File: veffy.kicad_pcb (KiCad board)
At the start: 4 copper layers, 83 parts, among them J1 SWD, Q1 2N7002, Q2 BFR93A, Q3 2N7002, Q4 BFR93AE6327HTSA1, U1 ATSAMD21G18A-A, U4 MC3361, U6 LM358_DFN, U7 AD9834, U8 QPA9510, Y2 TCXO-14

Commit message: rx pre-selector done
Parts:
- added C41: 100pF, Capacitor_SMD:C_0603_1608Metric, F.Cu at (116.0, 69.1)
- added L10: 13nH, Inductor_SMD:L_0603_1608Metric, F.Cu at (116.0, 71.6)
- added L15: 280nH, Inductor_SMD:L_0603_1608Metric, F.Cu at (116.0, 74.1)
- C20: value 30pF -> 10.9pF
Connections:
- net ANT renamed Net-(J2-In)
- C20 pad 1: Net-(C19-Pad1) -> AGND
- C20 pad 2: AGND -> TX_BAND_INT
- D2 pad 1: Net-(Q1-G) -> Net-(Q1-S)
- L4 pad 2: Net-(Q1-S) -> Net-(Q1-D)
- Q1 pad 1: Net-(Q1-G) -> RX_EN
- Q1 pad 3: RX_EN -> Net-(Q1-D)
- U8 pad 10: unconnected-(U8-RFOUT-Pad10) -> PA_DIE_OUT
- U8 pad 11: unconnected-(U8-RFOUT-Pad11) -> PA_DIE_OUT
- U8 pad 12: unconnected-(U8-RFOUT-Pad12) -> PA_DIE_OUT
- U8 pad 15: unconnected-(U8-APC2-Pad15) -> Net-(U8-APC2)
- U8 pad 16: unconnected-(U8-APC1-Pad16) -> Net-(U8-APC1)
- U8 pad 17: unconnected-(U8-EP-Pad17) -> AGND
- U8 pad 3: BAND_OUT -> Net-(U8-RFIN)
- U8 pad 5: unconnected-(U8-VCC2-Pad5) -> Net-(L10-Pad1)
- U8 pad 9: unconnected-(U8-RFOUT-Pad9) -> PA_DIE_OUT

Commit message: usb c done
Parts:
- added C43: 35.4pF, Capacitor_SMD:C_0603_1608Metric_Pad1.08x0.95mm_HandSolder, F.Cu at (96.1, 80.1)
- added C44: 10.9pF, Capacitor_SMD:C_0603_1608Metric_Pad1.08x0.95mm_HandSolder, F.Cu at (96.1, 82.6)
- added C45: C, Capacitor_SMD:C_0603_1608Metric_Pad1.08x0.95mm_HandSolder, F.Cu at (96.1, 85.1)
- added C46: 22pF, Capacitor_SMD:C_0603_1608Metric_Pad1.08x0.95mm_HandSolder, F.Cu at (96.1, 87.6)
- added C47: 27pF, Capacitor_SMD:C_0603_1608Metric_Pad1.08x0.95mm_HandSolder, F.Cu at (96.1, 90.1)
- added C48: 2pF, Capacitor_SMD:C_0603_1608Metric_Pad1.08x0.95mm_HandSolder, F.Cu at (100.4, 80.1)
- added C49: 56pF, Capacitor_SMD:C_0603_1608Metric_Pad1.08x0.95mm_HandSolder, F.Cu at (100.4, 82.6)
- added C50: 0.7pF, Capacitor_SMD:C_0603_1608Metric_Pad1.08x0.95mm_HandSolder, F.Cu at (100.4, 85.1)
- added CN1: XH-2AW_C2908611, LCSC:CONN-TH_XH-2AW_C2908611, F.Cu at (98.2, 92.7)
- added J3: USB_C_Receptacle_USB2.0_14P, Connector_USB:USB_C_Receptacle_HRO_TYPE-C-31-M-17, F.Cu at (112.8, 83.8)
- added L1: HCCF2-455.000-LTWCDL, LCSC:FILTER-SMD_4P-L11.9-W6.5-P5.50-LS7.5-BL, F.Cu at (109.1, 95.8)
- added L11: 71.5nH, Inductor_SMD:L_0603_1608Metric, F.Cu at (91.9, 80.1)
- added L12: 71.5nH, Inductor_SMD:L_0603_1608Metric, F.Cu at (91.9, 82.6)
- added L13: 1uH, Inductor_SMD:L_0603_1608Metric, F.Cu at (91.9, 85.1)
- added L14: 2.7nH, Inductor_SMD:L_0603_1608Metric, F.Cu at (91.9, 87.6)
- added L16: 280nH, Inductor_SMD:L_0603_1608Metric, F.Cu at (91.9, 90.1)
- added LRFC1: 10uH, Inductor_SMD:L_0603_1608Metric, F.Cu at (91.9, 92.6)
- added LRFC2: 1uH, Inductor_SMD:L_0603_1608Metric, F.Cu at (91.9, 95.1)
- added R23: 1.8K, Resistor_SMD:R_0603_1608Metric_Pad0.98x0.95mm_HandSolder, F.Cu at (100.4, 87.6)
- added R24: 10K, Resistor_SMD:R_0603_1608Metric_Pad0.98x0.95mm_HandSolder, F.Cu at (100.4, 90.1)
- added R25: 10K, Resistor_SMD:R_0603_1608Metric_Pad0.98x0.95mm_HandSolder, F.Cu at (104.8, 80.1)
- added R26: 1.8K, Resistor_SMD:R_0603_1608Metric_Pad0.98x0.95mm_HandSolder, F.Cu at (104.8, 82.6)
- added R27: 5.1K, Resistor_SMD:R_0603_1608Metric_Pad0.98x0.95mm_HandSolder, F.Cu at (104.8, 85.1)
- added R28: 5.1K, Resistor_SMD:R_0603_1608Metric_Pad0.98x0.95mm_HandSolder, F.Cu at (104.8, 87.6)
- C36, C37, C38, C39, C40, C41: footprint Capacitor_SMD:C_0603_1608Metric -> Capacitor_SMD:C_0603_1608Metric_Pad1.08x0.95mm_HandSolder
- L7: value 13nH -> 12nH
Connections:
- net Net-(Q1-S) renamed RX_RF
- D2 pad 2: Net-(Q3-G) -> Net-(Q3-S)
- L5 pad 2: Net-(Q3-S) -> Net-(Q3-D)
- Q3 pad 1: Net-(Q3-G) -> TX_EN
- Q3 pad 3: TX_EN -> Net-(Q3-D)
- R12 pad 2: DVDD -> DDS_RST
- U1 pad 22: unconnected-(U1-PA13-Pad22) -> TX_EN
- U1 pad 25: unconnected-(U1-PA16-Pad25) -> MOSI
- U1 pad 26: unconnected-(U1-PA17-Pad26) -> SCK
- U1 pad 27: unconnected-(U1-PA18-Pad27) -> GPIO_CS
- U1 pad 28: unconnected-(U1-PA19-Pad28) -> FSYNC
- U1 pad 31: unconnected-(U1-PA22-Pad31) -> DDS_RST
- U1 pad 32: unconnected-(U1-PA23-Pad32) -> RX_EN
- U1 pad 33: unconnected-(U1-PA24-Pad33) -> D-
- U1 pad 34: unconnected-(U1-PA25-Pad34) -> D+
- U7 pad 11: DVDD -> DDS_RST

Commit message: uuh, idr what I added. I think the LDO
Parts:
- added D3: 1N5819, Diode_THT:D_DO-41_SOD81_P10.16mm_Horizontal, F.Cu at (105.7, 107.0)
- added U10: MC34063AD, Package_SO:SOIC-8_3.9x4.9mm_P1.27mm, F.Cu at (113.2, 112.5)
- added U11: AP2112K-3.3, Package_TO_SOT_SMD:SOT-23-5, F.Cu at (106.4, 116.2)
- added U9: MCP73831-2-OT, Package_TO_SOT_SMD:SOT-23-5, F.Cu at (106.4, 111.5)
- C45: value C -> 0.1uF
- L15: value 280nH -> 150uH
- Y2: value TCXO-14 -> C7527392; footprint Oscillator:Oscillator_DIP-14 -> LCSC:OSC-SMD_4P-L2.0-W1.6-BL_EPSON_TG-5006CJ-19H
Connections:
- CN1 pad 1: unconnected-(CN1-Pad1) -> BAT+
- CN1 pad 2: unconnected-(CN1-Pad2) -> AGND
- L15 pad 1: RX_EN -> SwC
- L15 pad 2: RX_MIX_INT -> BAT+
- R27 pad 2: AVDD1 -> AGND
- R28 pad 1: AVDD1 -> AGND
- U1 pad 24: unconnected-(U1-PA15-Pad24) -> Net-(U1-PA15)

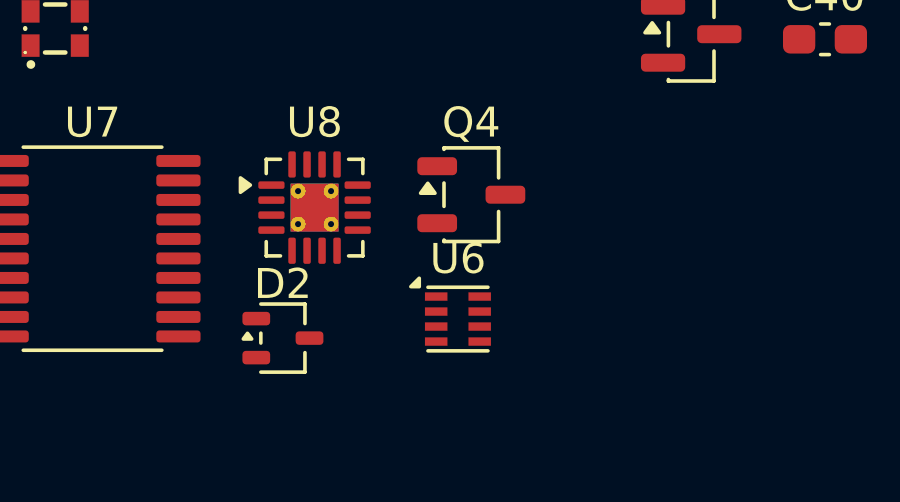
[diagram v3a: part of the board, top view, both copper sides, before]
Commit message: VCO tank is fixed and PLL loop is finished
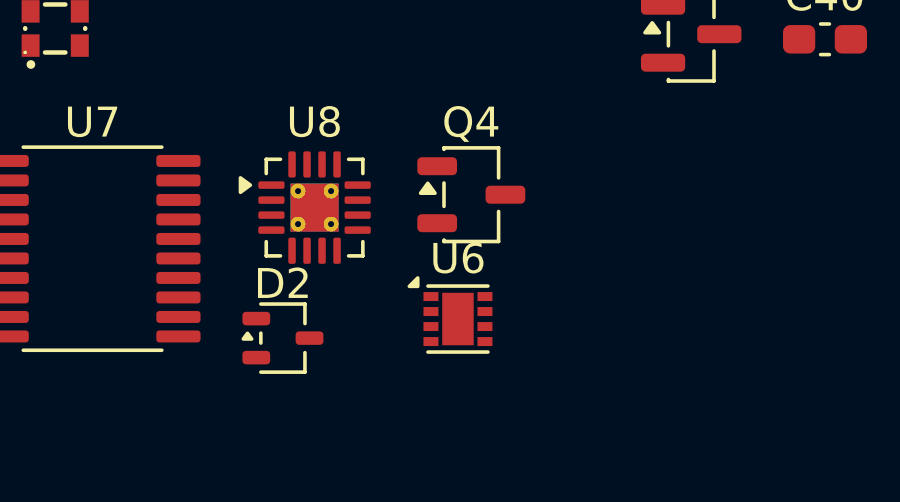
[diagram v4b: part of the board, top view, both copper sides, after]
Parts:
- C26: value 27pF -> 15pF
- U6: footprint Package_CSP:LFCSP-8_2x2mm_P0.5mm -> Package_DFN_QFN:DFN-8-1EP_2x2mm_P0.5mm_EP1.05x1.75mm
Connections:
- C2 pad 2: Net-(C2-Pad2) -> DVDD
- C22 pad 1: unconnected-(C22-Pad1) -> Net-(C22-Pad1)
- C25 pad 2: Net-(U6A-+) -> Net-(U6B-+)
- C3 pad 2: Net-(C3-Pad2) -> DVDD
- C38 pad 1: unconnected-(C38-Pad1) -> Net-(C38-Pad1)
- LRFC2 pad 2: Net-(LRFC2-Pad2) -> Net-(C38-Pad1)
- Q4 pad 3: Net-(LRFC2-Pad2) -> Net-(C38-Pad1)
- R4 pad 1: unconnected-(R4-Pad1) -> SPEAKER
- R6 pad 1: Net-(U6A--) -> Net-(U6B--)
- R7 pad 1: Net-(U6A--) -> Net-(U6B--)
- U1 pad 17: Net-(C3-Pad2) -> DVDD
- U1 pad 36: Net-(C2-Pad2) -> DVDD
- U6 pad 1: PRE_AMP -> Net-(U6A--)
- U6 pad 3: Net-(U6A-+) -> AGND
- U6 pad 4: (no net) -> AGND
- U6 pad 5: (no net) -> Net-(U6B-+)
- U6 pad 6: (no net) -> Net-(U6B--)
- U6 pad 7: (no net) -> PRE_AMP
- U6 pad 8: (no net) -> DVDD
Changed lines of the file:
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@@
 				(font
 					(size 1.27 1.27)
+					(thickness 0.15)
 				)
 			)
@@
 			(layers "F.Cu" "F.Mask" "F.Paste")
 			(roundrect_rratio 0.25)
-			(net "Net-(C3-Pad2)")
+			(net "DVDD")
 			(pinfunction "VDDIO_17")
 			(pintype "power_in")
@@
 			(layers "F.Cu" "F.Mask" "F.Paste")
 			(roundrect_rratio 0.25)
-			(net "Net-(C2-Pad2)")
+			(net "DVDD")
 			(pinfunction "VDDIO_36")
 			(pintype "power_in")
@@
 				(font
 					(size 1.27 1.27)
+					(thickness 0.15)
 				)
 			)
@@
 			(layers "F.Cu" "F.Mask" "F.Paste")
 			(roundrect_rratio 0.25)
-			(net "Net-(U6A--)")
+			(net "Net-(U6B--)")
 			(pintype "passive")
 		)
@@
 			(layers "F.Cu" "F.Mask" "F.Paste")
 			(roundrect_rratio 0.25)
-			(net "unconnected-(C38-Pad1)")
+			(net "Net-(C38-Pad1)")
 			(pintype "passive")
 		)
@@
 		)
 	)
-	(footprint "Package_CSP:LFCSP-8_2x2mm_P0.5mm"
+	(footprint "Package_DFN_QFN:DFN-8-1EP_2x2mm_P0.5mm_EP1.05x1.75mm"
 		(layer "F.Cu")
 		(at 136.7925 113.695)
-		(descr "LFCSP 8pin Pitch 0.5mm, http://www.analog.com/media/en/package-pcb-resources/package/pkg_pdf/lfcspcp/cp_8_6.pdf")
-		(tags "LFCSP 8pin 2x2mm Pitch 0.5mm")
+		(descr "DFN8 2x2, 0.5P; CASE 506CN (see ON Semiconductor 506CN.PDF)")
+		(tags "DFN 0.5")
 		(property "Reference" "U6"
 			(at 0 -2 0)
@@
 		(duplicate_pad_numbers_are_jumpers no)
 		(fp_line
-			(start 1 -1.06)
-			(end -1 -1.06)
+			(start -1 -1.1)
+			(end 1 -1.1)
 			(stroke
 				(width 0.12)
@@
 		)
 		(fp_line
-			(start 1 1.06)
-			(end -1 1.06)
+			(start -1 1.1)
+			(end 1 1.1)
 			(stroke
 				(width 0.12)
@@
 		(fp_poly
 			(pts
-				(xy -1.29 -1.08) (xy -1.57 -1.08) (xy -1.29 -1.36) (xy -1.29 -1.08)
+				(xy -1.34 -1.09) (xy -1.62 -1.09) (xy -1.34 -1.37) (xy -1.34 -1.09)
 			)
 			(stroke
@@
 		)
 		(fp_line
-			(start -1.4 -1.3)
-			(end 1.4 -1.3)
+			(start -1.4 -1.25)
+			(end -1.4 1.25)
 			(stroke
 				(width 0.05)
@@
 		)
 		(fp_line
-			(start -1.4 1.3)
-			(end -1.4 -1.3)
+			(start -1.4 -1.25)
+			(end 1.4 -1.25)
 			(stroke
 				(width 0.05)
@@
 		)
 		(fp_line
-			(start 1.4 -1.3)
-			(end 1.4 1.3)
+			(start -1.4 1.25)
+			(end 1.4 1.25)
 			(stroke
 				(width 0.05)
@@
 		)
 		(fp_line
-			(start 1.4 1.3)
-			(end -1.4 1.3)
+			(start 1.4 -1.25)
+			(end 1.4 1.25)
 			(stroke
 				(width 0.05)
@@
 		(fp_line
 			(start -1 -0.5)
-			(end -1 1)
+			(end -0.5 -1)
 			(stroke
 				(width 0.1)
@@
 		)
 		(fp_line
-			(start -0.5 -1)
+			(start -1 1)
 			(end -1 -0.5)
 			(stroke
@@
 		)
 		(fp_line
-			(start 1 1)
-			(end -1 1)
+			(start 1 -1)
+			(end 1 1)
 			(stroke
 				(width 0.1)
@@
 		(fp_line
 			(start 1 1)
-			(end 1 -1)
+			(end -1 1)
 			(stroke
 				(width 0.1)
@@
 		)
 		(fp_text user "${REFERENCE}"
-			(at 0 0 180)
+			(at 0 0 0)
 			(layer "F.Fab")
 			(effects
 				(font
-					(size 1 1)
-					(thickness 0.15)
+					(size 0.5 0.5)
+					(thickness 0.075)
 				)
 			)
 		)
+		(pad "" smd rect
+			(at 0 -0.4375)
+			(size 0.85 0.65)
+			(layers "F.Paste")
+		)
+		(pad "" smd rect
+			(at 0 0.4375)
+			(size 0.85 0.65)
+			(layers "F.Paste")
+		)
 		(pad "1" smd rect
-			(at -0.725 -0.75)
-			(size 0.75 0.28)
+			(at -0.9 -0.75)
+			(size 0.5 0.3)
 			(layers "F.Cu" "F.Mask" "F.Paste")
-			(net "PRE_AMP")
+			(net "Net-(U6A--)")
 			(pintype "output")
 		)
 		(pad "2" smd rect
-			(at -0.725 -0.25)
-			(size 0.75 0.28)
+			(at -0.9 -0.25)
+			(size 0.5 0.3)
 			(layers "F.Cu" "F.Mask" "F.Paste")
 			(net "Net-(U6A--)")
@@
 		)
 		(pad "3" smd rect
-			(at -0.725 0.25)
-			(size 0.75 0.28)
+			(at -0.9 0.25)
+			(size 0.5 0.3)
 			(layers "F.Cu" "F.Mask" "F.Paste")
-			(net "Net-(U6A-+)")
+			(net "AGND")
 			(pinfunction "+_3")
 			(pintype "input")
 		)
 		(pad "4" smd rect
-			(at -0.725 0.75)
-			(size 0.75 0.28)
+			(at -0.9 0.75)
+			(size 0.5 0.3)
 			(layers "F.Cu" "F.Mask" "F.Paste")
+			(net "AGND")
+			(pinfunction "V-_4")
+			(pintype "power_in")
 		)
 		(pad "5" smd rect
-			(at 0.725 0.75)
-			(size 0.75 0.28)
+			(at 0.9 0.75)
+			(size 0.5 0.3)
 			(layers "F.Cu" "F.Mask" "F.Paste")
+			(net "Net-(U6B-+)")
+			(pinfunction "+_5")
+			(pintype "input")
 		)
 		(pad "6" smd rect
-			(at 0.725 0.25)
-			(size 0.75 0.28)
+			(at 0.9 0.25)
+			(size 0.5 0.3)
 			(layers "F.Cu" "F.Mask" "F.Paste")
+			(net "Net-(U6B--)")
+			(pinfunction "-_6")
+			(pintype "input")
 		)
 		(pad "7" smd rect
-			(at 0.725 -0.25)
-			(size 0.75 0.28)
+			(at 0.9 -0.25)
+			(size 0.5 0.3)
 			(layers "F.Cu" "F.Mask" "F.Paste")
+			(net "PRE_AMP")
+			(pintype "output")
 		)
 		(pad "8" smd rect
-			(at 0.725 -0.75)
-			(size 0.75 0.28)
+			(at 0.9 -0.75)
+			(size 0.5 0.3)
 			(layers "F.Cu" "F.Mask" "F.Paste")
+			(net "DVDD")
+			(pinfunction "V+_8")
+			(pintype "power_in")
+		)
+		(pad "9" smd rect
+			(at 0 0)
+			(size 1.05 1.75)
+			(layers "F.Cu" "F.Mask")
+			(net "unconnected-(U6C-PAD-Pad9)")
+			(pinfunction "PAD_9")
+			(pintype "power_in+no_connect")
 		)
 		(embedded_fonts no)
-		(model "${KICAD10_3DMODEL_DIR}/Package_CSP.3dshapes/LFCSP-8_2x2mm_P0.5mm.step"
+		(model "${KICAD10_3DMODEL_DIR}/Package_DFN_QFN.3dshapes/DFN-8-1EP_2x2mm_P0.5mm_EP1.05x1.75mm.step"
 			(offset
 				(xyz 0 0 0)
@@
 			(layers "F.Cu" "F.Mask" "F.Paste")
 			(roundrect_rratio 0.25)
-			(net "Net-(LRFC2-Pad2)")
+			(net "Net-(C38-Pad1)")
 			(pintype "unspecified")
 		)
@@
 			)
 		)
-		(property "Value" "27pF"
+		(property "Value" "15pF"
 			(at 0 1.43 0)
 			(layer "F.Fab")
@@
 			(layers "F.Cu" "F.Mask" "F.Paste")
 			(roundrect_rratio 0.25)
-			(net "unconnected-(C22-Pad1)")
+			(net "Net-(C22-Pad1)")
 			(pintype "passive")
 		)
@@
 			(layers "F.Cu" "F.Mask" "F.Paste")
 			(roundrect_rratio 0.25)
-			(net "Net-(LRFC2-Pad2)")
+			(net "Net-(C38-Pad1)")
 			(pinfunction "2_2")
 			(pintype "passive")
@@
 			(layers "F.Cu" "F.Mask" "F.Paste")
 			(roundrect_rratio 0.25)
-			(net "Net-(U6A-+)")
+			(net "Net-(U6B-+)")
 			(pintype "passive")
 		)
@@
 			(layers "F.Cu" "F.Mask" "F.Paste")
 			(roundrect_rratio 0.25)
-			(net "Net-(C2-Pad2)")
+			(net "DVDD")
 			(pintype "passive")
 		)
@@
 			(layers "F.Cu" "F.Mask" "F.Paste")
 			(roundrect_rratio 0.25)
-			(net "Net-(U6A--)")
+			(net "Net-(U6B--)")
 			(pintype "passive")
 		)
@@
 			(layers "F.Cu" "F.Mask" "F.Paste")
 			(roundrect_rratio 0.25)
-			(net "unconnected-(R4-Pad1)")
+			(net "SPEAKER")
 			(pintype "passive")
 		)
@@
 			(layers "F.Cu" "F.Mask" "F.Paste")
 			(roundrect_rratio 0.25)
-			(net "Net-(C3-Pad2)")
+			(net "DVDD")
 			(pintype "passive")
 		)

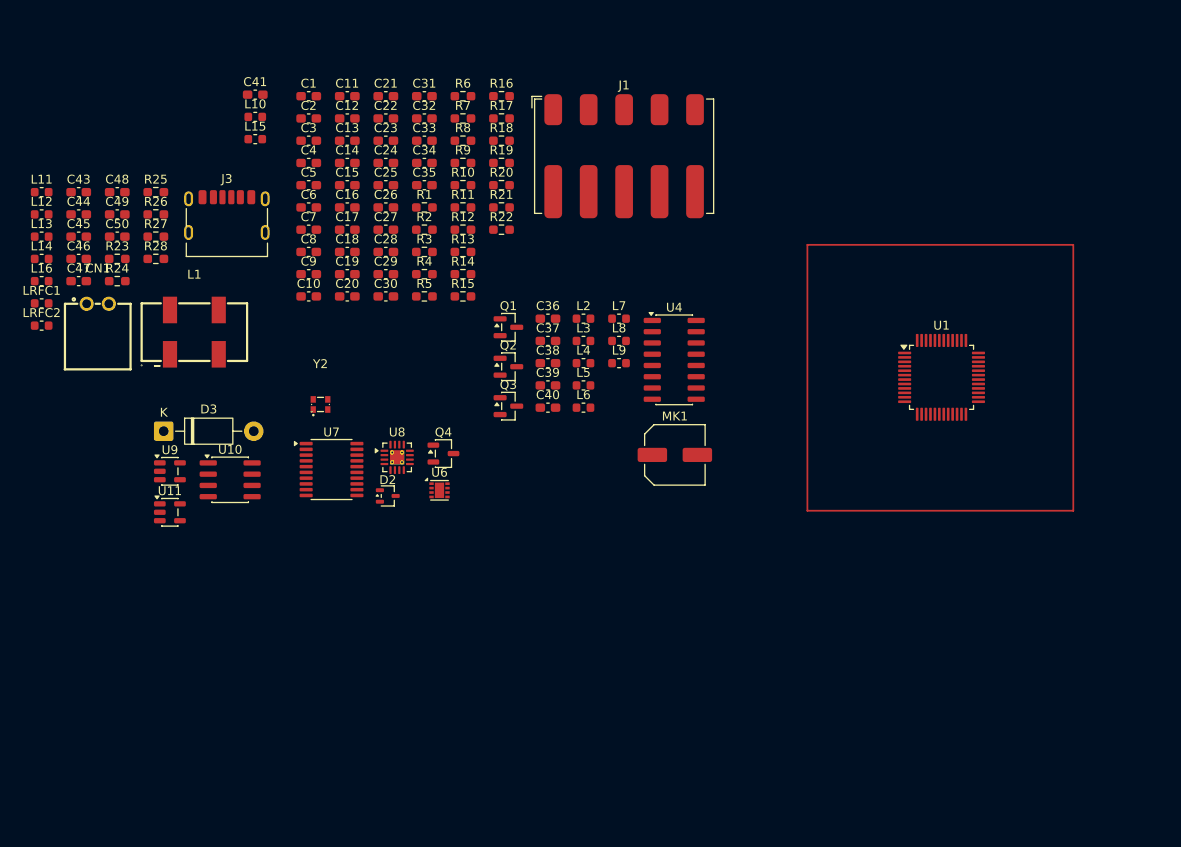
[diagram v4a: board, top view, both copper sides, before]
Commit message: fixed footprints and some schematic errors
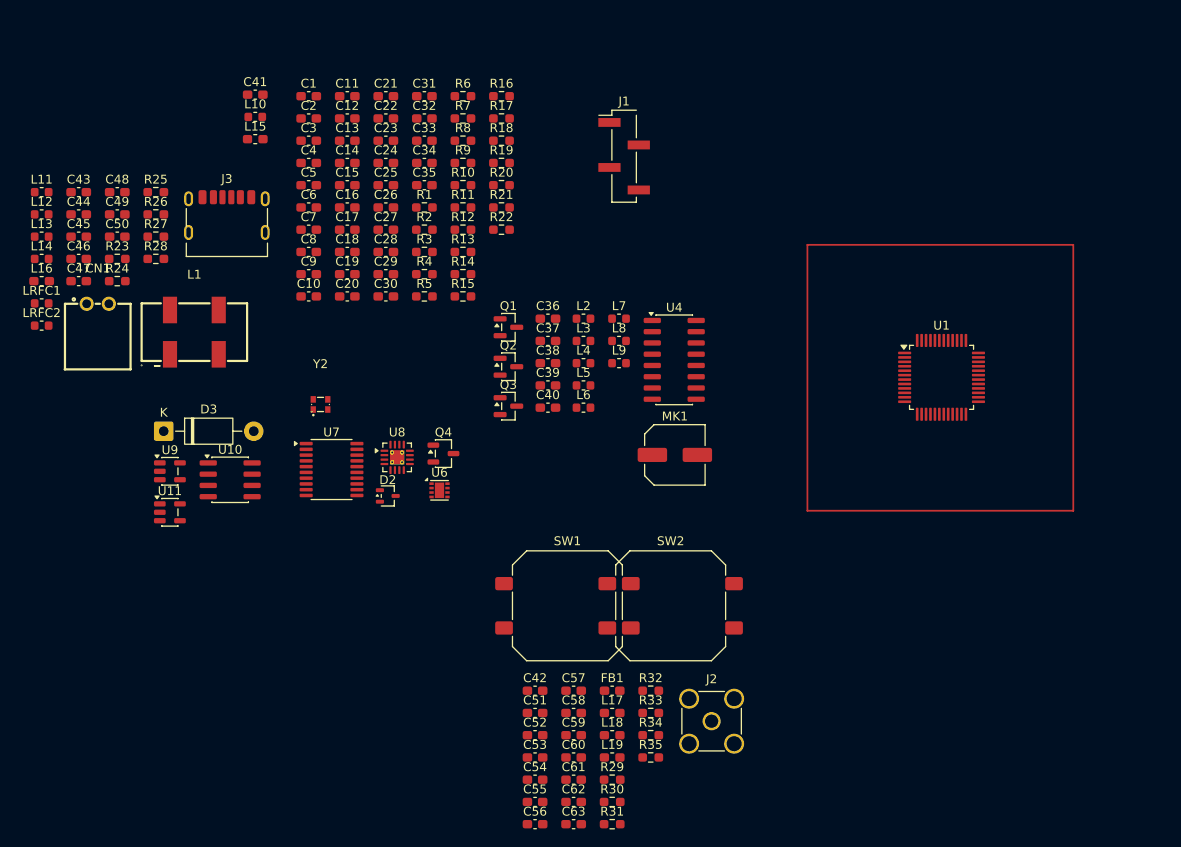
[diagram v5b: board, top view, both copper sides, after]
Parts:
- added C42: 30pF, Capacitor_SMD:C_0603_1608Metric_Pad1.08x0.95mm_HandSolder, F.Cu at (147.6, 136.3)
- added C51: 4.7uF, Capacitor_SMD:C_0603_1608Metric_Pad1.08x0.95mm_HandSolder, F.Cu at (147.6, 138.8)
- added C52: 4.7uF, Capacitor_SMD:C_0603_1608Metric_Pad1.08x0.95mm_HandSolder, F.Cu at (147.6, 141.3)
- added C53: 1000pF, Capacitor_SMD:C_0603_1608Metric_Pad1.08x0.95mm_HandSolder, F.Cu at (147.6, 143.8)
- added C54: 470uF, Capacitor_SMD:C_0603_1608Metric_Pad1.08x0.95mm_HandSolder, F.Cu at (147.6, 146.3)
- added C55: 1uF, Capacitor_SMD:C_0603_1608Metric_Pad1.08x0.95mm_HandSolder, F.Cu at (147.6, 148.9)
- added C56: 1uF, Capacitor_SMD:C_0603_1608Metric_Pad1.08x0.95mm_HandSolder, F.Cu at (147.6, 151.4)
- added C57: 27pF, Capacitor_SMD:C_0603_1608Metric_Pad1.08x0.95mm_HandSolder, F.Cu at (151.9, 136.3)
- added C58: 27pF, Capacitor_SMD:C_0603_1608Metric_Pad1.08x0.95mm_HandSolder, F.Cu at (151.9, 138.8)
- added C59: 6.8nF, Capacitor_SMD:C_0603_1608Metric_Pad1.08x0.95mm_HandSolder, F.Cu at (151.9, 141.3)
- added C60: 0.8pF, Capacitor_SMD:C_0603_1608Metric_Pad1.08x0.95mm_HandSolder, F.Cu at (151.9, 143.8)
- added C61: 0.8pF, Capacitor_SMD:C_0603_1608Metric_Pad1.08x0.95mm_HandSolder, F.Cu at (151.9, 146.3)
- added C62: 27pF, Capacitor_SMD:C_0603_1608Metric_Pad1.08x0.95mm_HandSolder, F.Cu at (151.9, 148.9)
- added C63: 68nF, Capacitor_SMD:C_0603_1608Metric_Pad1.08x0.95mm_HandSolder, F.Cu at (151.9, 151.4)
- added FB1: FerriteBead, Capacitor_SMD:C_0603_1608Metric_Pad1.08x0.95mm_HandSolder, F.Cu at (156.3, 136.3)
- added J2: Conn_Coaxial, Connector_Coaxial:SMA_Amphenol_901-144_Vertical, F.Cu at (167.5, 139.7)
- added L17: 0603CS-33NXJLW, Inductor_SMD:L_0603_1608Metric_Pad1.05x0.95mm_HandSolder, F.Cu at (156.3, 138.8)
- added L18: 0603CS-33NXJLW, Inductor_SMD:L_0603_1608Metric_Pad1.05x0.95mm_HandSolder, F.Cu at (156.3, 141.3)
- added L19: 0603CS-33NXJLW, Inductor_SMD:L_0603_1608Metric_Pad1.05x0.95mm_HandSolder, F.Cu at (156.3, 143.8)
- added R29: 2K, Resistor_SMD:R_0603_1608Metric_Pad0.98x0.95mm_HandSolder, F.Cu at (156.3, 146.3)
- added R30: 10K, Resistor_SMD:R_0603_1608Metric_Pad0.98x0.95mm_HandSolder, F.Cu at (156.3, 148.9)
- added R31: 0.62, Resistor_SMD:R_0603_1608Metric_Pad0.98x0.95mm_HandSolder, F.Cu at (156.3, 151.4)
- added R32: 1.2K, Resistor_SMD:R_0603_1608Metric_Pad0.98x0.95mm_HandSolder, F.Cu at (160.6, 136.3)
- added R33: 3.6K, Resistor_SMD:R_0603_1608Metric_Pad0.98x0.95mm_HandSolder, F.Cu at (160.6, 138.8)
- added R34: 47K, Resistor_SMD:R_0603_1608Metric_Pad0.98x0.95mm_HandSolder, F.Cu at (160.6, 141.3)
- added R35: 3.9K, Resistor_SMD:R_0603_1608Metric_Pad0.98x0.95mm_HandSolder, F.Cu at (160.6, 143.8)
- added SW1: SW_Push, Button_Switch_SMD:SW_Push_1P1T_NO_CK_PTS125Sx43SMTR, F.Cu at (151.2, 126.7)
- added SW2: SW_Push, Button_Switch_SMD:SW_Push_1P1T_NO_CK_PTS125Sx43SMTR, F.Cu at (162.9, 126.7)
- J1: footprint Connector_TE-Connectivity:TE_2834006-5_1x05_P4.0mm_Horizontal -> Connector_PinHeader_2.54mm:PinHeader_1x04_P2.54mm_Vertical_SMD_Pin1Left
- L15, L16: footprint Inductor_SMD:L_0603_1608Metric -> Inductor_SMD:L_0603_1608Metric_Pad1.05x0.95mm_HandSolder
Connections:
- U4 pad 10: FILTER_INT -> unconnected-(U4-FILTER_INT-Pad10)

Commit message: worked on the PCB and fixed some schematic issues
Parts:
- moved U1 13.0 mm to (199.1, 112.7)
- moved R16 7.17 mm to (147.1, 62.8)
- moved R17 7.17 mm to (147.1, 65.3)
- moved R18 7.17 mm to (147.1, 67.9)
- moved R19 7.17 mm to (147.1, 70.4)
- moved R20 7.17 mm to (147.1, 72.9)
- moved R21 7.17 mm to (147.1, 75.4)
- moved R22 7.17 mm to (147.1, 77.9)
- moved C1 7.17 mm to (125.3, 62.8)
- moved C11 7.17 mm to (129.7, 62.8)
- moved C12 7.17 mm to (129.7, 65.3)
- moved C13 7.17 mm to (129.7, 67.9)
- moved C14 7.17 mm to (129.7, 70.4)
- moved C15 7.17 mm to (129.7, 72.9)
- moved C16 7.17 mm to (129.7, 75.4)
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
